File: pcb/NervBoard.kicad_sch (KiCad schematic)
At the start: 43 parts, among them J1 Conn_01x08_Pin, J2 Conn_01x08_Pin, Q0 2N7000, Q1 SFH309, Q2 2N7000, Q3 AO3400A, U1 ESP32-CAM, U2 LM1085-5.0

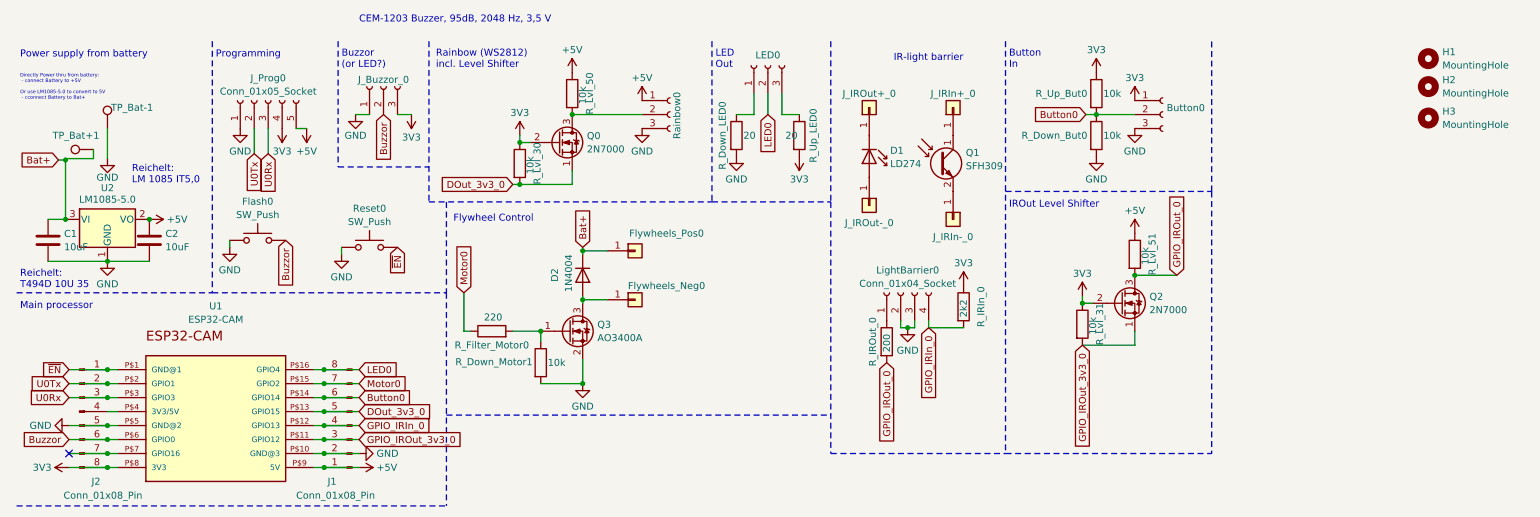
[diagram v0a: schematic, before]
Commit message: Improved board to a stable version
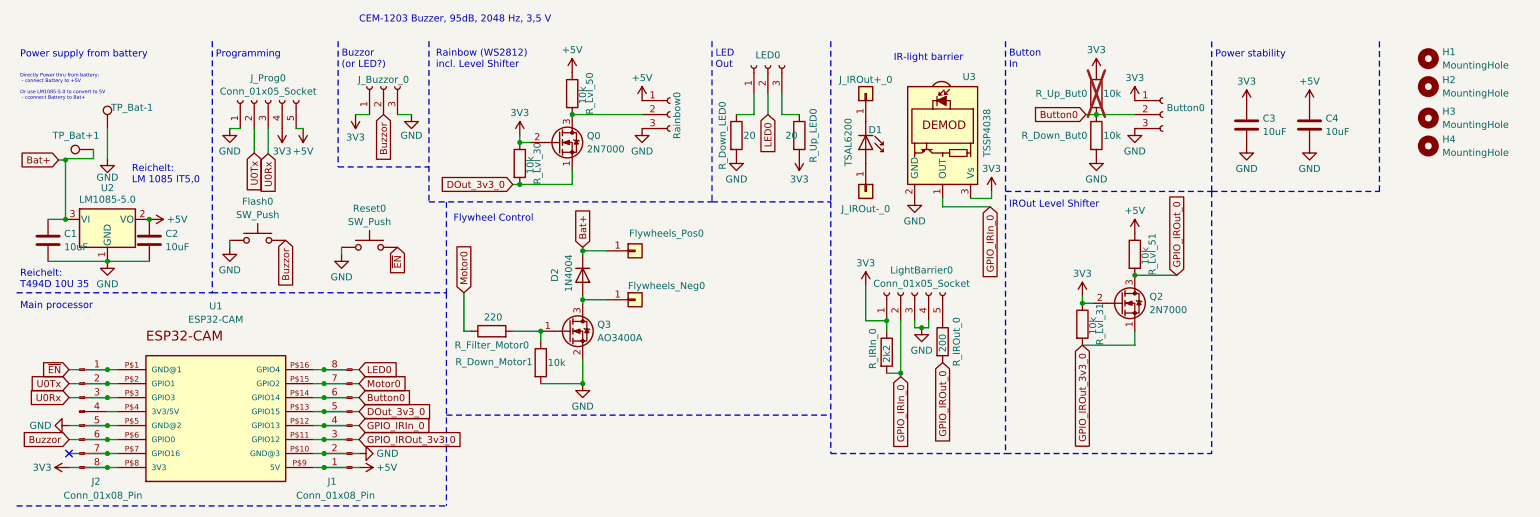
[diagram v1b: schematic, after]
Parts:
- removed J_IRIn+_0: ~, symbol Connector_Generic:Conn_01x01
- removed J_IRIn-_0: Conn_01x01, symbol Connector_Generic:Conn_01x01
- removed Q1: SFH309, symbol Sensor_Optical:SFH309
- added C3, C4: 10uF, Capacitor_Tantalum_SMD:CP_EIA-6032-15_Kemet-U_Pad2.25x2.35mm_HandSolder, symbol Device:C
- added H4: MountingHole, PhilsLibs:MountingHole__Langloch_3.2mm_M3, symbol Mechanical:MountingHole
- added U3: TSSP4038, symbol Interface_Optical:TSOP41xx
- Button0, LED0: MPN (none) -> BG302-03-A-L-G; now left out of the parts list
- C1, C2: MPN (none) -> T491U106K020AT
- D1: value LD274 -> TSAL6200; MPN (none) -> TSAL6200
- D2: MPN (none) -> 1N4004-B
- Flash0, Reset0: MPN (none) -> TS02-66-43-BK-160-SCR-D
- Flywheels_Neg0: footprint TestPoint:TestPoint_Pad_2.0x2.0mm -> TestPoint:TestPoint_THTPad_3.0x3.0mm_Drill1.5mm; now left out of the parts list
- Flywheels_Pos0: footprint TestPoint:TestPoint_Pad_2.0x2.0mm -> TestPoint:TestPoint_THTPad_D3.0mm_Drill1.5mm; now left out of the parts list
- H1, H2, H3, J_IROut+_0, J_IROut-_0, TP_Bat+1, TP_Bat-1: now left out of the parts list
- J1, J2: MPN (none) -> SL-108-TT-11
- J_Buzzor_0: footprint Connector_PinSocket_2.54mm:PinSocket_1x03_P2.54mm_Vertical -> PhilsLibs:PinSocket_1x03_P2.54mm_Horizontal_NoPrint; MPN (none) -> BG302-03-A-L-G
- J_Prog0: footprint Connector_PinSocket_2.54mm:PinSocket_1x05_P2.54mm_Vertical -> PhilsLibs:PinSocket_1x05_P2.54mm_Horizontal_NoPrint; MPN (none) -> BG302-05-A-L-G
- LightBarrier0: value Conn_01x04_Socket -> Conn_01x05_Socket; footprint Connector_PinSocket_2.54mm:PinSocket_1x04_P2.54mm_Vertical -> PhilsLibs:PinSocket_1x05_P2.54mm_Horizontal_NoPrint; symbol Connector:Conn_01x04_Socket -> Connector:Conn_01x05_Socket; MPN (none) -> BG302-05-A-L-G
- Q0, Q2: MPN (none) -> 2N7000TA
- Q3: MPN (none) -> AO3400A
- R_Down_But0, R_Down_Motor1, R_Lvl_30, R_Lvl_31, R_Lvl_50, R_Lvl_51: MPN (none) -> RT0805FRE0710KL
- R_Down_LED0, R_Up_LED0: MPN (none) -> RT0805FRE0720RL
- R_Filter_Motor0: MPN (none) -> RT0805FRE07220RL
- R_IRIn_0: MPN (none) -> RT0805FRE072K2L
- R_IROut_0: MPN (none) -> RT0805FRE07200RL
- R_Up_But0: MPN (none) -> RT0805FRE0710KL; now not fitted; now left out of the parts list
- Rainbow0: footprint Connector_PinHeader_2.54mm:PinHeader_1x03_P2.54mm_Vertical -> PhilsLibs:PinSocket_1x03_P2.54mm_Horizontal_NoPrint; MPN (none) -> BG302-03-A-L-G
- U1: MPN (none) -> ESP32-CAM
- U2: MPN (none) -> LM1085IT-5.0/NOPB
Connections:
- net +5V: now also C4.1
- net 3V3: now also J_Buzzor_0.1 (Pin_1), LightBarrier0.1 (Pin_1), C3.1, U3.3 (Vs); no longer J_Buzzor_0.3 (Pin_3)
- net GND: now also J_Buzzor_0.3 (Pin_3), LightBarrier0.4 (Pin_4), C3.2, C4.2, U3.2 (GND); no longer J_Buzzor_0.1 (Pin_1), LightBarrier0.2 (Pin_2)
- net GPIO_IRIn_0: now also LightBarrier0.2 (Pin_2), U3.1 (OUT); no longer LightBarrier0.4 (Pin_4)
- net at R_IROut_0.1: now also LightBarrier0.5 (Pin_5); no longer LightBarrier0.1 (Pin_1)
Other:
- note added: "Power stability"
- moved on the sheet: D1, J_IROut+_0, J_IROut-_0, R_IRIn_0, R_IROut_0
